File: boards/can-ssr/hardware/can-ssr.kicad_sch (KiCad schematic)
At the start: 0 parts

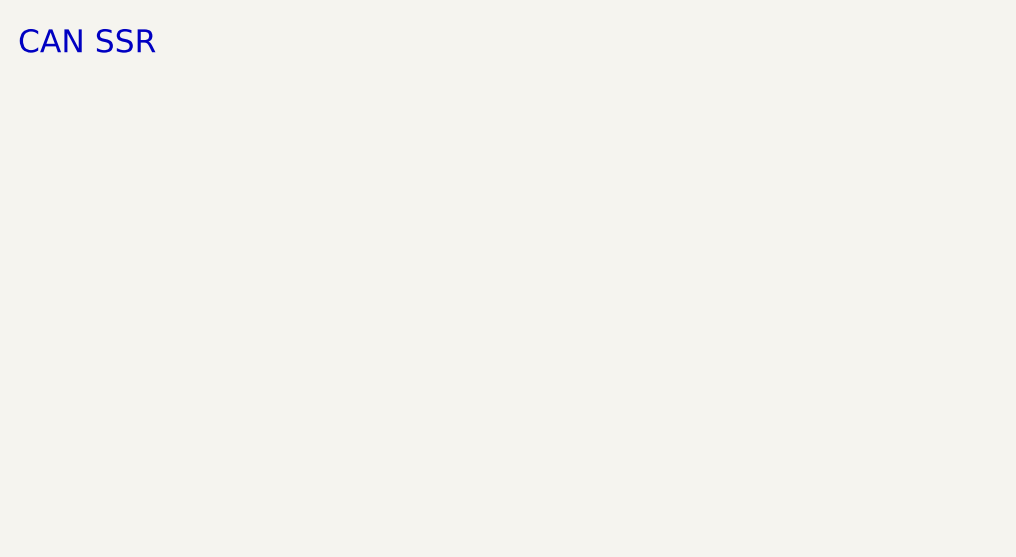
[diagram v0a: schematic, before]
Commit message: can-ssr schematic: root sheet and CAN/power/MCU block
- Hierarchical schematic; can_logic.kicad_sch holds the CAN connectors
  (Phoenix MC 3.5 mm, daisy chain), MCP2562FD-E/P, NUP2105L ESD, jumpered
  120 R termination, reverse-polarity diode + TVS + R-78E5.0-1.0 supply,
  12 V monitor, PIC18F47Q84-I/P with 16 MHz crystal, ICSP and debug UART
  headers, hex address switch, status/fault LEDs
- Inter-block nets are global labels (ERC isolated_pin_label until the
  other blocks exist)
- gen_schematic.py bootstrap generator (initial capture only)
- Library imports for these parts; lib tables synced
- Requirements: CAN connector and pinout, rotary address switch

Co-Authored-By: Claude Opus 5.5 <noreply@anthropic.com>
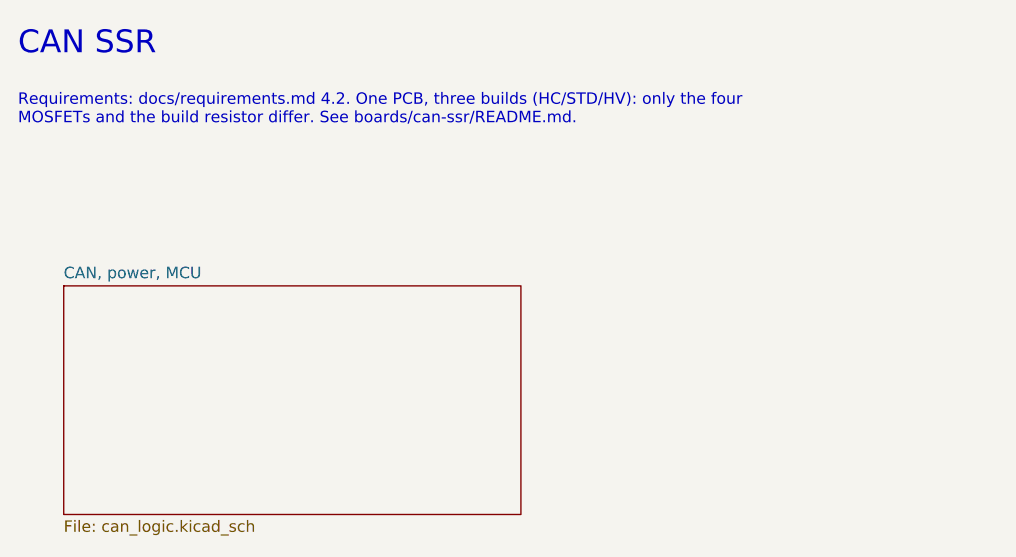
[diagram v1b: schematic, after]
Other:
- added sheet CAN, power, MCU (can_logic.kicad_sch)
- note added: "Requirements: docs/requirements.md 4.2. One PCB, three builds (HC/STD/HV): only the four MOSFETs and the build resistor differ. See boards/can-ssr/README.md."
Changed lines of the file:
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@@
+		)
+	)
+	(text "Requirements: docs/requirements.md 4.2. One PCB, three builds (HC/STD/HV): only the four\nMOSFETs and the build resistor differ. See boards/can-ssr/README.md."
+		(exclude_from_sim no)
+		(at 25.4 38.1 0)
+		(effects
+			(font
+				(size 1.27 1.27)
+			)
+			(justify left bottom)
+		)
+	)
+	(sheet
+		(at 30.48 55.88)
+		(size 50.8 25.4)
+		(exclude_from_sim no)
+		(in_bom yes)
+		(on_board yes)
+		(dnp no)
+		(fields_autoplaced yes)
+		(stroke
+			(width 0.1524)
+			(type solid)
+		)
+		(fill
+			(color 0 0 0 0.0000)
+		)
+		(property "Sheetname" "CAN, power, MCU"
+			(at 30.48 55.18 0)
+			(effects
+				(font
+					(size 1.27 1.27)
+				)
+				(justify left bottom)
+			)
+		)
+		(property "Sheetfile" "can_logic.kicad_sch"
+			(at 30.48 81.88 0)
+			(effects
+				(font
+					(size 1.27 1.27)
+				)
+				(justify left top)
+			)
+		)
+		(instances
+			(project "can-ssr"
+				(path "/09b96810-cbdb-496a-83a0-e49ecf8d36fe"
+					(page "2")
+				)
+			)
 		)
 	)

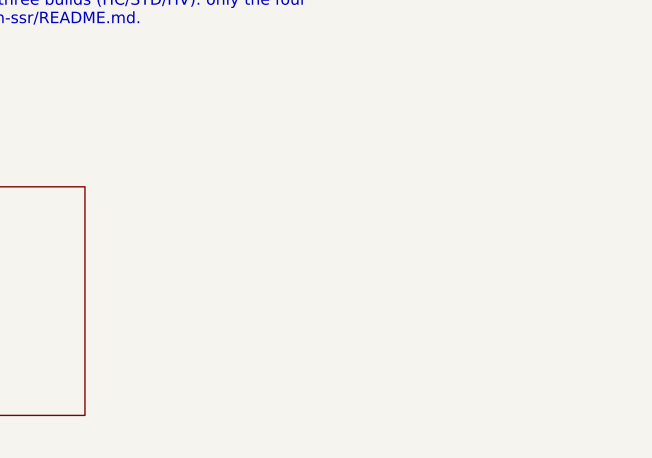
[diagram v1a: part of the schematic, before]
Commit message: can-ssr schematic: power path block
- 4 x D2PAK N-MOSFETs back to back (common source), per-gate 10R, 15 V
  Zener + 10M, PNP turn-off accelerator, C10/D12/R15 hot-turn-on slew
  limiter, 2 x VOM1271T in series, ACS770ECB-100U, ES3J freewheel diode,
  four M5 bolt pads (supply +/-, load +/-)
- MOSFET symbols carry a Build field (HC/STD/HV parts); STD part is the
  MPN default
- Thl_Isolator:VOM1271T symbol and Thl_Package Vishay SOP-4 hand-solder
  footprint (generator in lib/footprint_src/Thl_Package; 3D model is the
  stock SOP-4 3.8x4.1 approximation)
- Stock imports: TO-263-2, Allegro_CB_PFF (no stock STEP), SOT-23 PNP,
  SMC/SOD-123 diodes, 1210 cap, M5 pad hole

Co-Authored-By: Claude Opus 5.5 <noreply@anthropic.com>
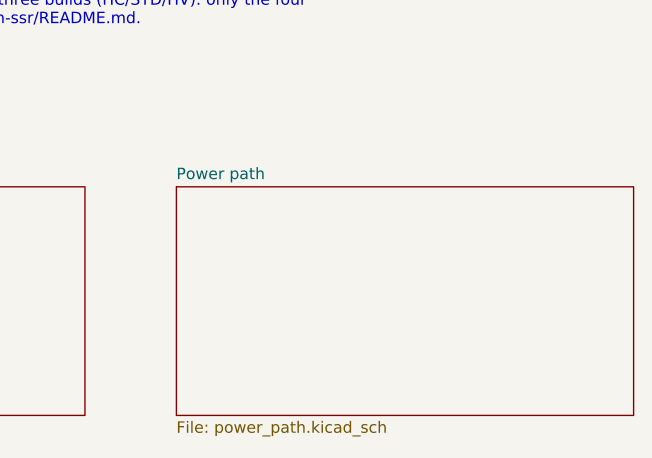
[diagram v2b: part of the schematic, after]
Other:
- added sheet Power path (power_path.kicad_sch)
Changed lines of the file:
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@@
+		)
+	)
+	(sheet
+		(at 91.44 55.88)
+		(size 50.8 25.4)
+		(exclude_from_sim no)
+		(in_bom yes)
+		(on_board yes)
+		(dnp no)
+		(fields_autoplaced yes)
+		(stroke
+			(width 0.1524)
+			(type solid)
+		)
+		(fill
+			(color 0 0 0 0.0000)
+		)
+		(property "Sheetname" "Power path"
+			(at 91.44 55.18 0)
+			(effects
+				(font
+					(size 1.27 1.27)
+				)
+				(justify left bottom)
+			)
+		)
+		(property "Sheetfile" "power_path.kicad_sch"
+			(at 91.44 81.88 0)
+			(effects
+				(font
+					(size 1.27 1.27)
+				)
+				(justify left top)
+			)
+		)
+		(instances
+			(project "can-ssr"
+				(path "/09b96810-cbdb-496a-83a0-e49ecf8d36fe"
+					(page "3")
+				)
+			)
 		)
 	)

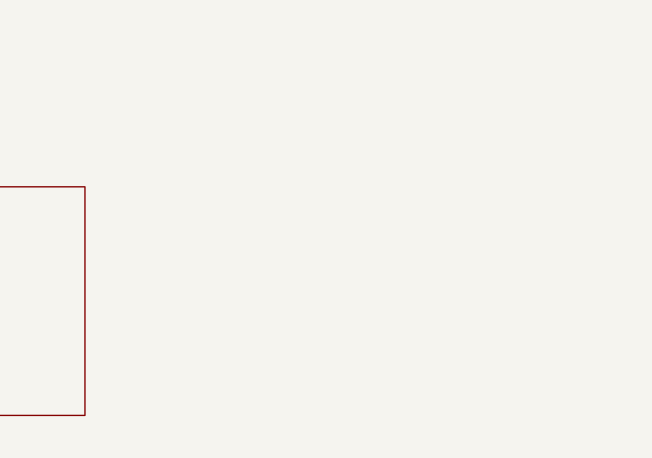
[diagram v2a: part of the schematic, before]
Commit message: can-ssr schematic: overcurrent trip and gate-drive block
- Build resistor R20 (HC 7.15k / STD 16.2k / HV 35.7k) over 10k sets the
  trip threshold Vth (60 / 35 / 15 A on the ACS770-100U) and is read by
  the PIC as BUILD_REF; open R20 = always tripped
- LM393B comparator on the filtered ACS770 output, latched by a BAT54
  that drags Vth below the 0.5 V zero-current level; TRIP_RST (2N7002)
  releases it
- VOM1271 LED string driven ~21 mA through two series 2N7002s:
  GATE_EN AND TRIP_OK, so firmware cannot override a hardware trip
- ACS770 ADC filter; PIC nets renamed ACS_ADC and TRIP_OK

Co-Authored-By: Claude Opus 5.5 <noreply@anthropic.com>
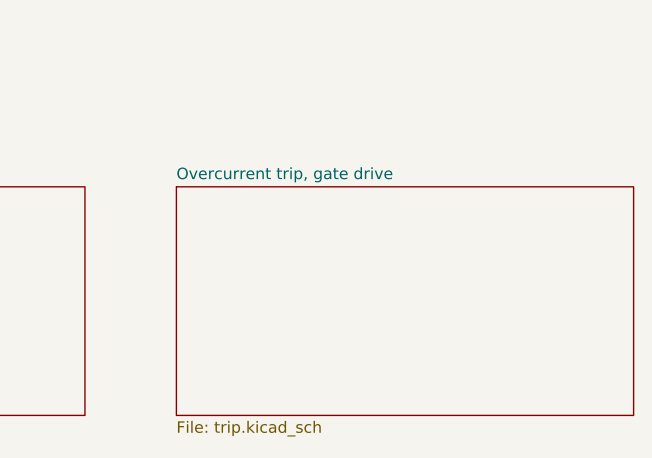
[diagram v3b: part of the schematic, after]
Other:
- added sheet Overcurrent trip, gate drive (trip.kicad_sch)
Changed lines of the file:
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@@
+		)
+	)
+	(sheet
+		(at 152.4 55.88)
+		(size 50.8 25.4)
+		(exclude_from_sim no)
+		(in_bom yes)
+		(on_board yes)
+		(dnp no)
+		(fields_autoplaced yes)
+		(stroke
+			(width 0.1524)
+			(type solid)
+		)
+		(fill
+			(color 0 0 0 0.0000)
+		)
+		(property "Sheetname" "Overcurrent trip, gate drive"
+			(at 152.4 55.18 0)
+			(effects
+				(font
+					(size 1.27 1.27)
+				)
+				(justify left bottom)
+			)
+		)
+		(property "Sheetfile" "trip.kicad_sch"
+			(at 152.4 81.88 0)
+			(effects
+				(font
+					(size 1.27 1.27)
+				)
+				(justify left top)
+			)
+		)
+		(instances
+			(project "can-ssr"
+				(path "/09b96810-cbdb-496a-83a0-e49ecf8d36fe"
+					(page "4")
+				)
+			)
 		)
 	)

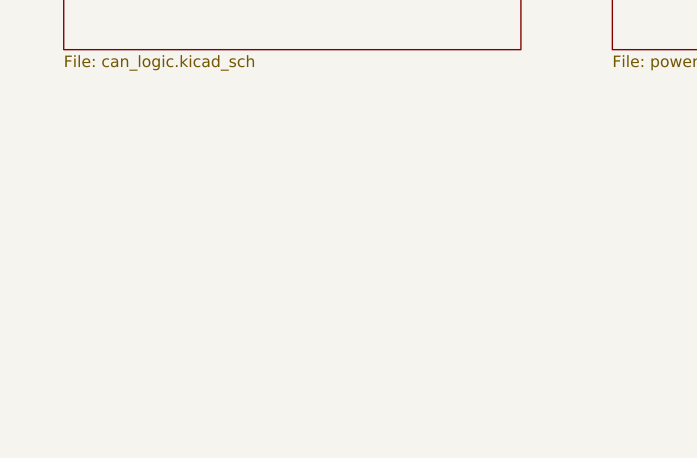
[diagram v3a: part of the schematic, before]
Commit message: can-ssr schematic: load-side sense and Mean Well control block
- UCC12050 isolated 5 V (reinforced) and ISO1640DWR I2C isolator (wide
  body, reinforced) are the only crossings into the load domain
- MCP3428 ADC: Vin and Vout through 3 x 332k / 8.06k dividers (250 V FS,
  ~200 Hz anti-aliasing), plus PV/PC readback at the terminal
- Two MCP4725 DACs (0x60, 0x61) drive the Mean Well PV and PC inputs via
  1k; TLP222A photorelay closes Remote ON/OFF, off at reset
- J30: 5-pole Phoenix MC 3.5 mm for the Mean Well control wires
- Load-side ground net renamed GND_LOAD (the RET return bar) so ERC
  recognises it as a ground
- New symbols Thl_Isolator:ISO1640DWR and UCC12050DVE from the TI
  datasheets; stock imports for MCP3428, MCP4725, TLP222A, SOIC-16W/14,
  SOT-23-6, DIP-4, 5-pole MC header

Co-Authored-By: Claude Opus 5.5 <noreply@anthropic.com>
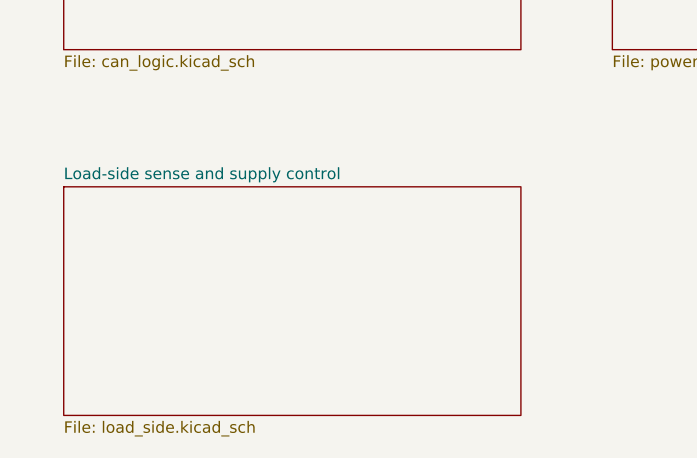
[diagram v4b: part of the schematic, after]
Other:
- added sheet Load-side sense and supply control (load_side.kicad_sch)
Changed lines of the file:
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@@
+		)
+	)
+	(sheet
+		(at 30.48 96.52)
+		(size 50.8 25.4)
+		(exclude_from_sim no)
+		(in_bom yes)
+		(on_board yes)
+		(dnp no)
+		(fields_autoplaced yes)
+		(stroke
+			(width 0.1524)
+			(type solid)
+		)
+		(fill
+			(color 0 0 0 0.0000)
+		)
+		(property "Sheetname" "Load-side sense and supply control"
+			(at 30.48 95.82 0)
+			(effects
+				(font
+					(size 1.27 1.27)
+				)
+				(justify left bottom)
+			)
+		)
+		(property "Sheetfile" "load_side.kicad_sch"
+			(at 30.48 122.52 0)
+			(effects
+				(font
+					(size 1.27 1.27)
+				)
+				(justify left top)
+			)
+		)
+		(instances
+			(project "can-ssr"
+				(path "/09b96810-cbdb-496a-83a0-e49ecf8d36fe"
+					(page "5")
+				)
+			)
 		)
 	)

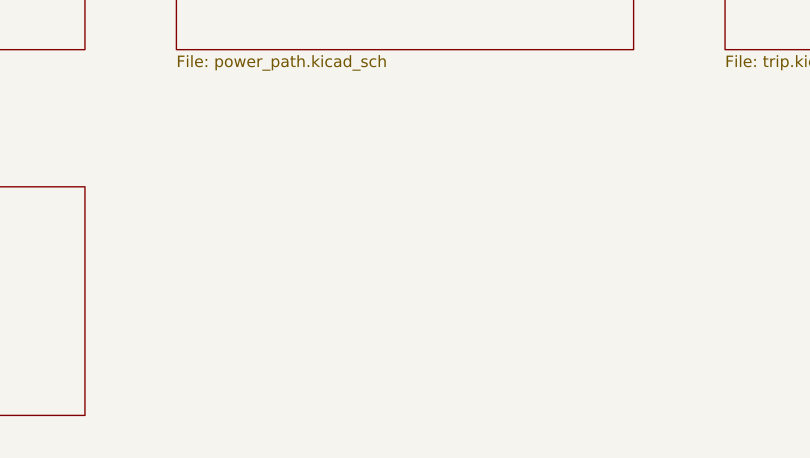
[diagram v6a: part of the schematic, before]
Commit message: can-ssr schematic: display block; schematic capture complete
- MAX7219CWG+ driving a Kingbright CC56-12SRWA 4-digit red display
  (RSET 27k, ~15 mA peak) plus V/A indicator LEDs on digit 4
- Bolt pads H1-H4 excluded from the BOM
- ERC: 0 violations across all six sheets; every assembled part has
  Manufacturer and MPN

Co-Authored-By: Claude Opus 5.5 <noreply@anthropic.com>
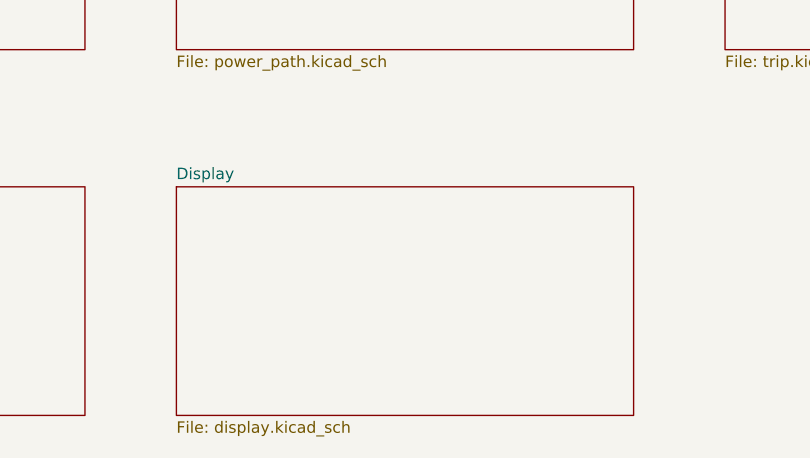
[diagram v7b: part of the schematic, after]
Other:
- added sheet Display (display.kicad_sch)
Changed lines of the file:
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@@
+		)
+	)
+	(sheet
+		(at 91.44 96.52)
+		(size 50.8 25.4)
+		(exclude_from_sim no)
+		(in_bom yes)
+		(on_board yes)
+		(dnp no)
+		(fields_autoplaced yes)
+		(stroke
+			(width 0.1524)
+			(type solid)
+		)
+		(fill
+			(color 0 0 0 0.0000)
+		)
+		(property "Sheetname" "Display"
+			(at 91.44 95.82 0)
+			(effects
+				(font
+					(size 1.27 1.27)
+				)
+				(justify left bottom)
+			)
+		)
+		(property "Sheetfile" "display.kicad_sch"
+			(at 91.44 122.52 0)
+			(effects
+				(font
+					(size 1.27 1.27)
+				)
+				(justify left top)
+			)
+		)
+		(instances
+			(project "can-ssr"
+				(path "/09b96810-cbdb-496a-83a0-e49ecf8d36fe"
+					(page "6")
+				)
+			)
 		)
 	)
